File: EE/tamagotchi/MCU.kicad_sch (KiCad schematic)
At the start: 0 parts

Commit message: Minor Update pre Display add
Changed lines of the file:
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@@
 	(generator_version "9.0")
 	(paper "A4")
+	(label "MOSI"
+		(at 273.05 40.64 180)
+		(effects
+			(font
+				(size 1.27 1.27)
+			)
+			(justify right bottom)
+		)
+	)
 	(label "VAPE_EN"
 		(at 273.05 25.4 180)
@@
 		)
 	)
+	(label "CS"
+		(at 273.05 45.72 180)
+		(effects
+			(font
+				(size 1.27 1.27)
+			)
+			(justify right bottom)
+		)
+	)
 	(label "CE_N"
 		(at 22.86 15.24 0)
@@
 		)
 	)
+	(label "SCK"
+		(at 273.05 43.18 180)
+		(effects
+			(font
+				(size 1.27 1.27)
+			)
+			(justify right bottom)
+		)
+	)
 	(label "RED_EN"
 		(at 273.05 22.86 180)
@@
 		)
 	)
+	(label "MISO"
+		(at 273.05 38.1 180)
+		(effects
+			(font
+				(size 1.27 1.27)
+			)
+			(justify right bottom)
+		)
+	)
+	(hierarchical_label "MOSI"
+		(shape input)
+		(at 273.05 40.64 0)
+		(fields_autoplaced yes)
+		(effects
+			(font
+				(size 1.27 1.27)
+			)
+			(justify left)
+		)
+		(property "Netclass" ""
+			(at 273.05 41.91 0)
+			(effects
+				(font
+					(size 1.27 1.27)
+					(italic yes)
+				)
+				(justify left)
+			)
+		)
+	)
 	(hierarchical_label "INT_N"
 		(shape input)
@@
 		)
 	)
+	(hierarchical_label "MISO"
+		(shape input)
+		(at 273.05 38.1 0)
+		(effects
+			(font
+				(size 1.27 1.27)
+			)
+			(justify left)
+		)
+	)
 	(hierarchical_label "YELLOW_EN"
 		(shape input)
@@
 		)
 	)
+	(hierarchical_label "SCK"
+		(shape input)
+		(at 273.05 43.18 0)
+		(fields_autoplaced yes)
+		(effects
+			(font
+				(size 1.27 1.27)
+			)
+			(justify left)
+		)
+		(property "Netclass" ""
+			(at 273.05 44.45 0)
+			(effects
+				(font
+					(size 1.27 1.27)
+					(italic yes)
+				)
+				(justify left)
+			)
+		)
+	)
+	(hierarchical_label "CS"
+		(shape input)
+		(at 273.05 45.72 0)
+		(fields_autoplaced yes)
+		(effects
+			(font
+				(size 1.27 1.27)
+			)
+			(justify left)
+		)
+		(property "Netclass" ""
+			(at 273.05 46.99 0)
+			(effects
+				(font
+					(size 1.27 1.27)
+					(italic yes)
+				)
+				(justify left)
+			)
+		)
+	)

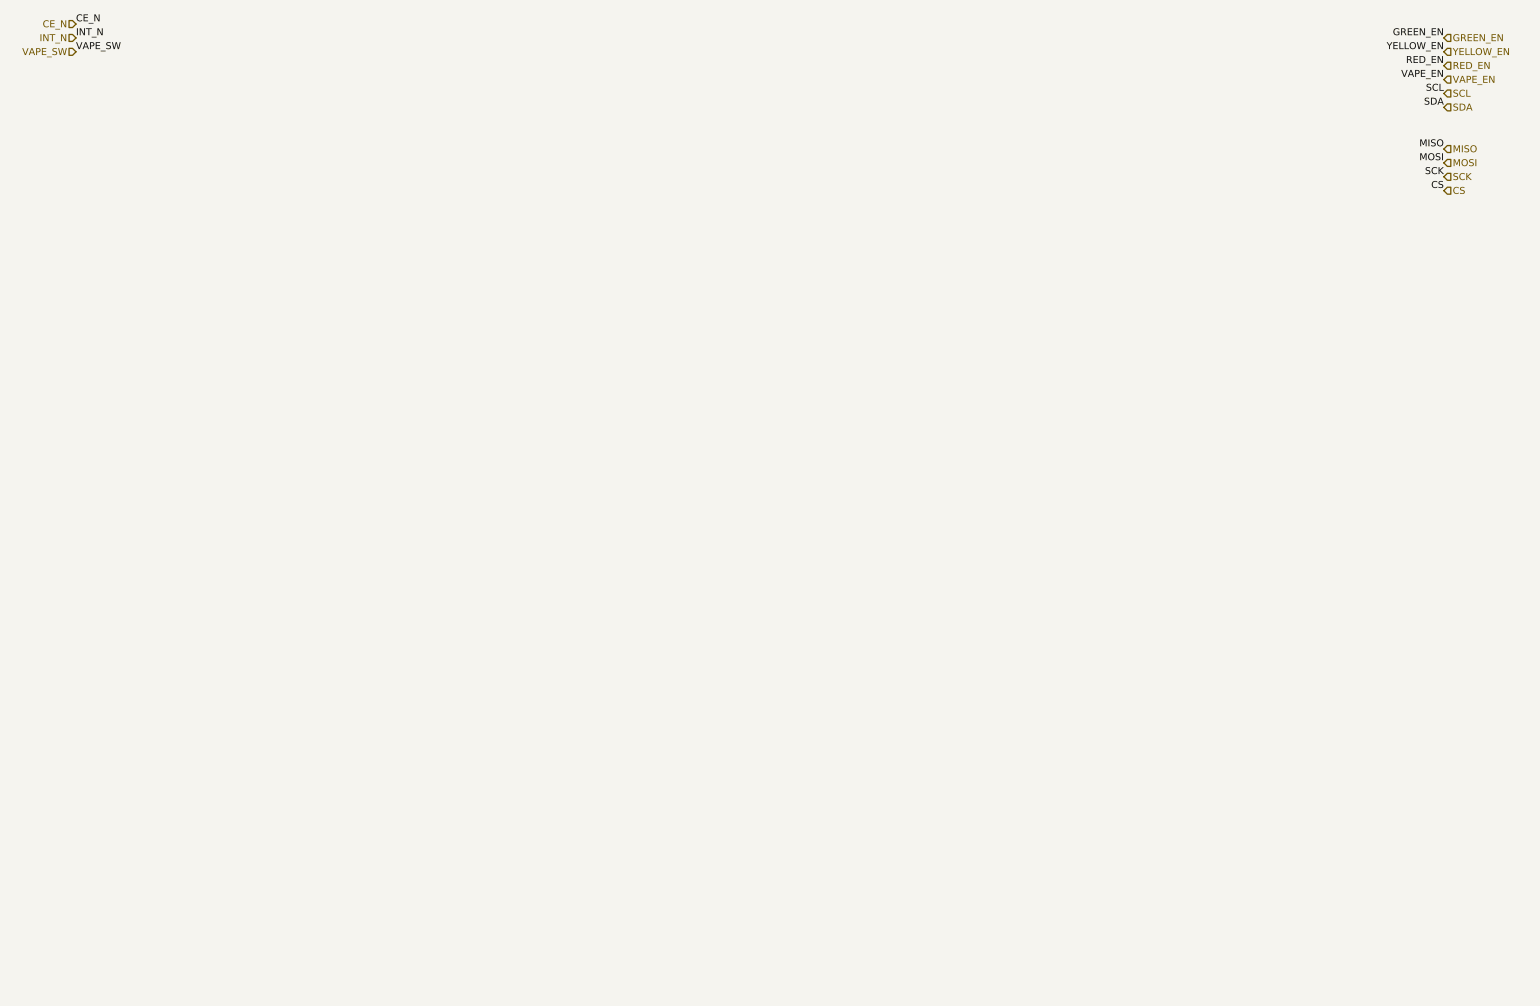
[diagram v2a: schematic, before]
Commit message: WIP - added 3D / footprints for devices. RGY LEDs aren't right
Need to do more outling / ect. super rough placement for everything.
LED footprint for RGY appears just wrong
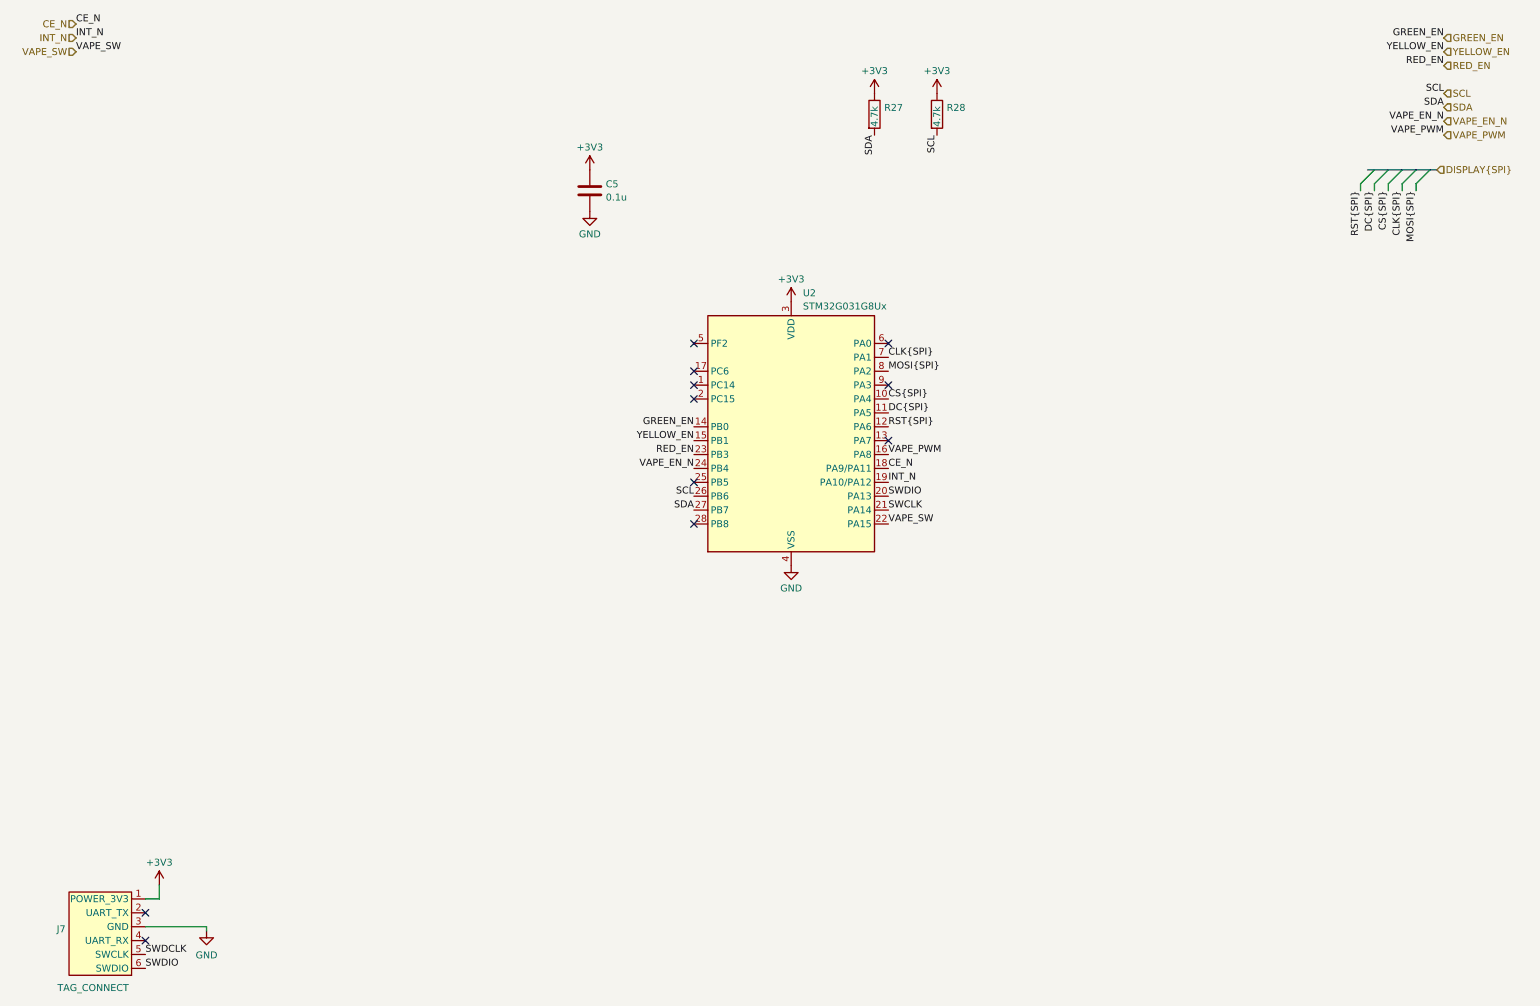
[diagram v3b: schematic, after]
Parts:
- added C5: 0.1u, Capacitor_SMD:C_0402_1005Metric_Pad0.74x0.62mm_HandSolder, symbol Device:C
- added J7: TAG_CONNECT, Connector:Tag-Connect_TC2030-IDC-FP_2x03_P1.27mm_Vertical, symbol ACTempDisconnect:TAG_CONNECT
- added R27, R28: 4.7k, Resistor_SMD:R_0402_1005Metric_Pad0.72x0.64mm_HandSolder, symbol Device:R
- added U2: STM32G031G8Ux, Package_DFN_QFN:QFN-28_4x4mm_P0.5mm, symbol MCU_ST_STM32G0:STM32G031G8Ux
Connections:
- net CE_N: now also U2.18 (PA9/PA11)
- net GREEN_EN: now also U2.14 (PB0)
- net INT_N: now also U2.19 (PA10/PA12)
- net RED_EN: now also U2.23 (PB3)
- net SCL: now also R28.2, U2.26 (PB6)
- net SDA: now also R27.2, U2.27 (PB7)
- net VAPE_SW: now also U2.22 (PA15)
- net YELLOW_EN: now also U2.15 (PB1)
- new net +3V3: C5.1, J7.1 (POWER_3V3), R27.1, R28.1, U2.3 (VDD)
- new net CLK{SPI}: U2.7 (PA1)
- new net CS{SPI}: U2.10 (PA4)
- new net DC{SPI}: U2.11 (PA5)
- new net GND: C5.2, J7.3 (GND), U2.4 (VSS)
- new net MOSI{SPI}: U2.8 (PA2)
- new net RST{SPI}: U2.12 (PA6)
- new net SWCLK: U2.21 (PA14)
- new net SWDCLK: J7.5 (SWCLK)
- new net SWDIO: J7.6 (SWDIO), U2.20 (PA13)
- new net VAPE_EN_N: U2.24 (PB4)
- new net VAPE_PWM: U2.16 (PA8)
- no-connect marks 0 -> 11

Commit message: Removed LEDs
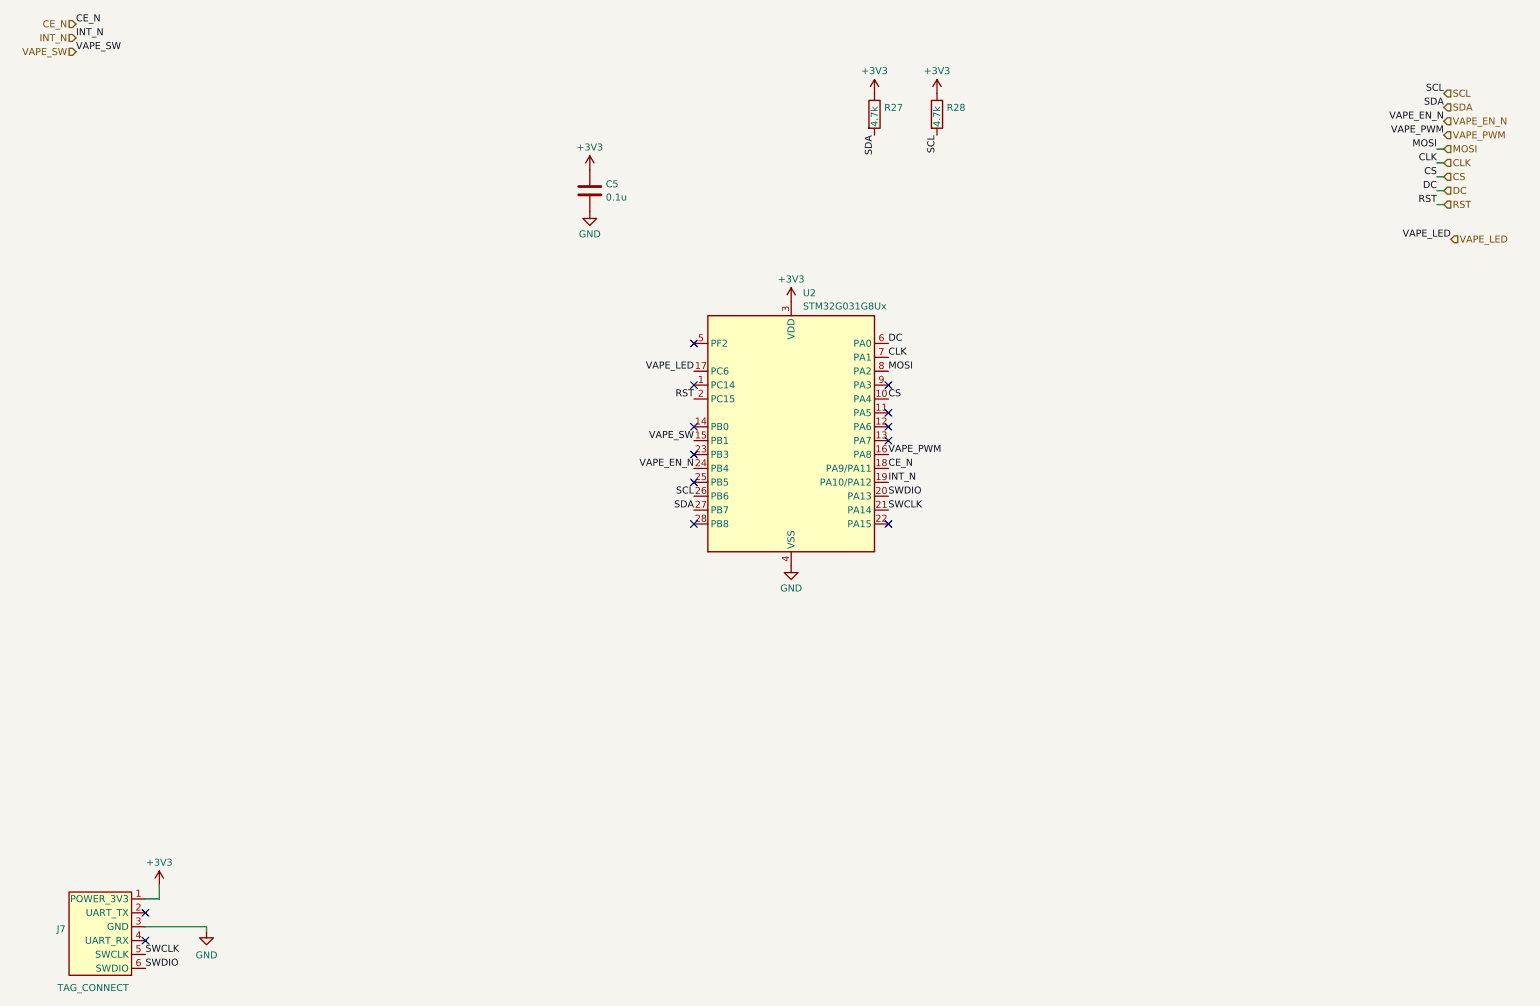
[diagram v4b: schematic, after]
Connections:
- net SWDCLK is gone; now on net SWCLK: J7.5 (SWCLK)
- net YELLOW_EN is gone; now on net VAPE_SW: U2.15 (PB1)
- net VAPE_SW: no longer U2.22 (PA15)
- net VAPE_LED: now reaches U2.17 (PC6)
- net RST: now reaches U2.2 (PC15)
- net DC: now reaches U2.6 (PA0)
- net CLK{SPI} renamed CLK
- net CS{SPI} renamed CS
- net DC{SPI}: no longer names the net of U2.11 (PA5)
- net GREEN_EN: no longer names the net of U2.14 (PB0)
- net MOSI{SPI} renamed MOSI
- net RED_EN: no longer names the net of U2.23 (PB3)
- net RST{SPI}: no longer names the net of U2.12 (PA6)
- no-connect marks 11 -> 13

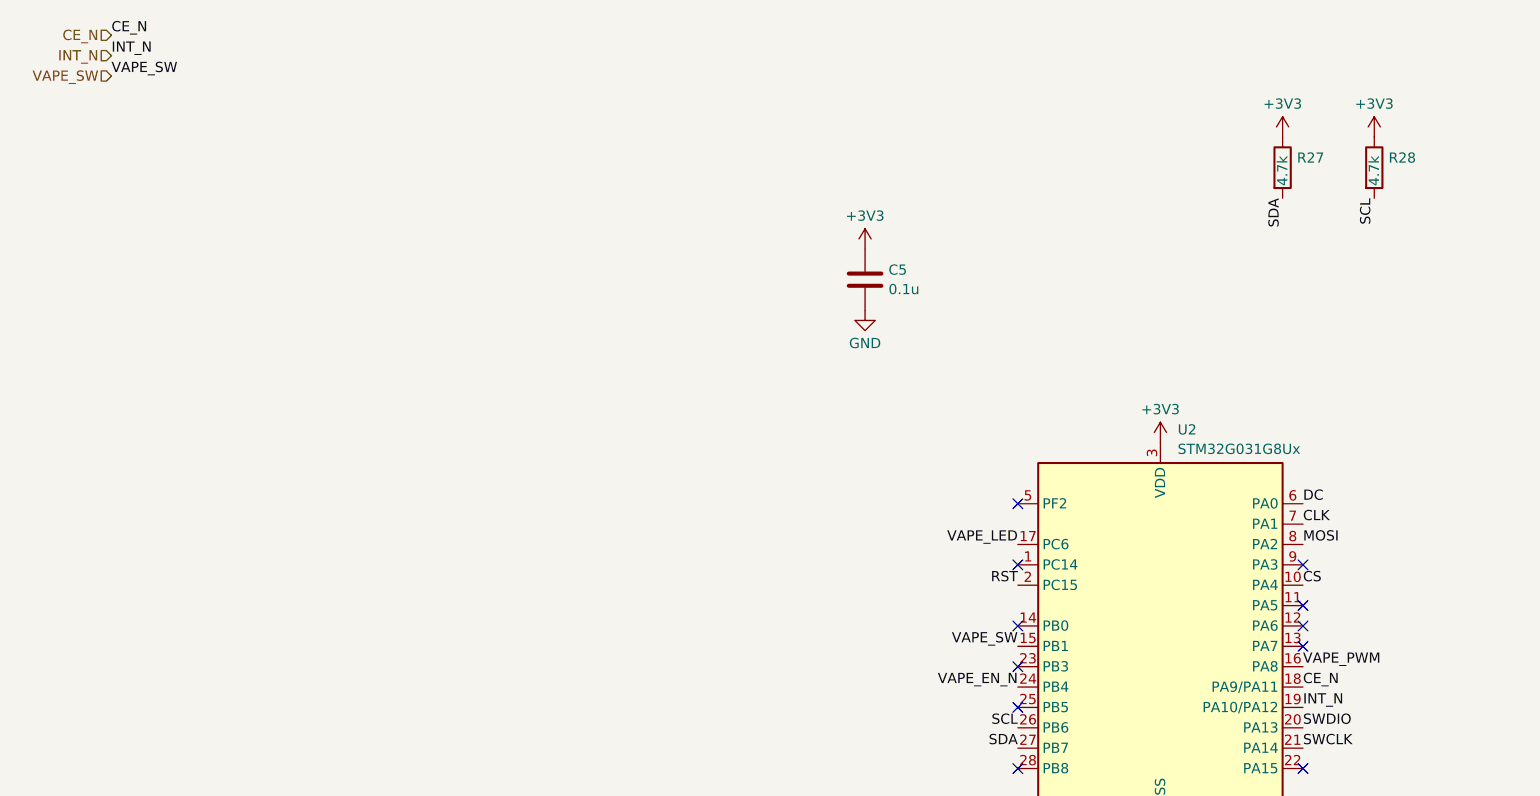
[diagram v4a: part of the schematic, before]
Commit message: First pass routing / placement & LED -> Buzzer for warning
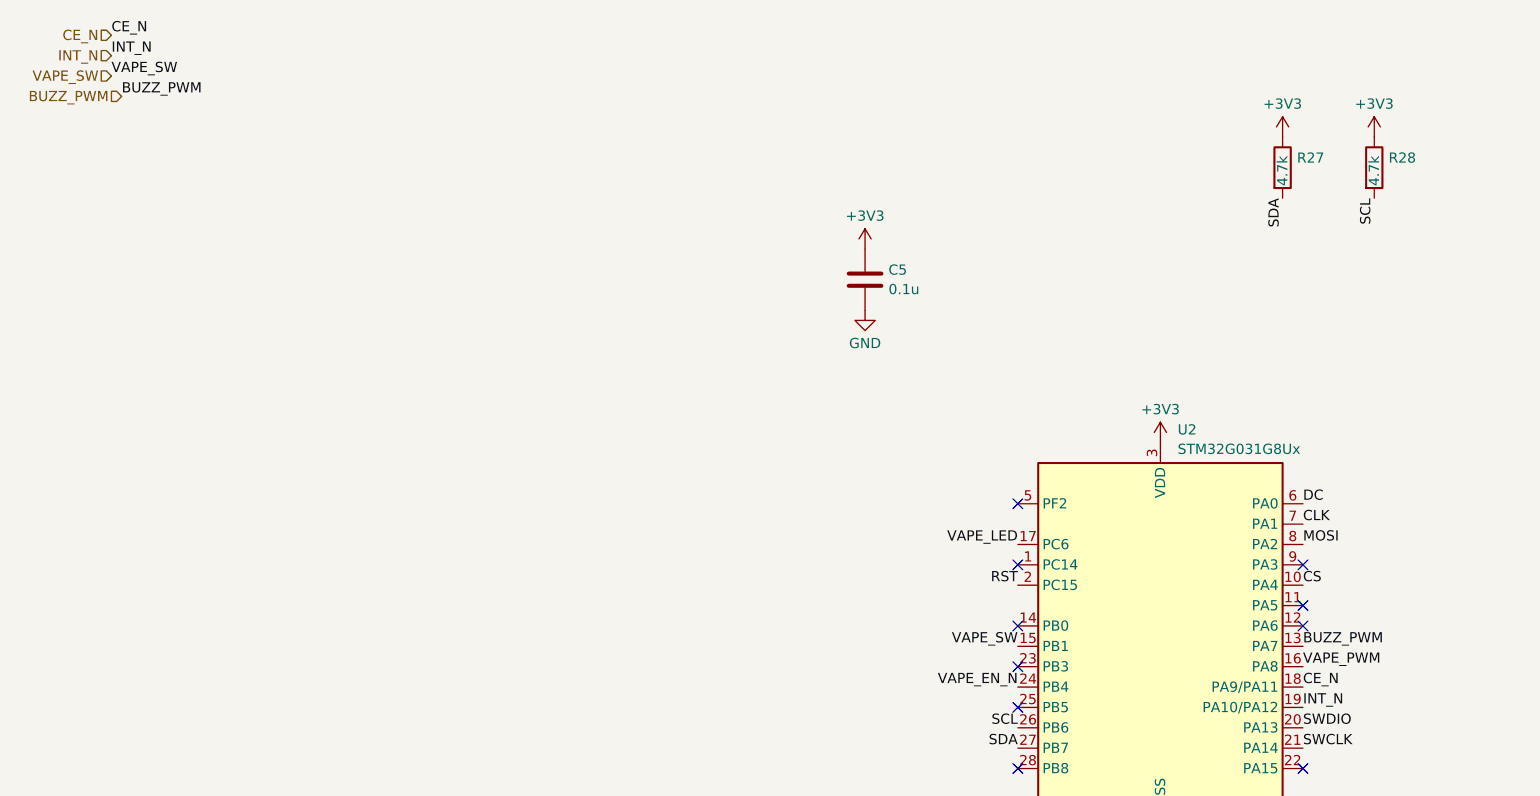
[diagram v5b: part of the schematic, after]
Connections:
- net BUZZ_PWM: now reaches U2.13 (PA7)
- no-connect marks 13 -> 12
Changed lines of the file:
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@@
-	)
-	(no_connect
-		(at 171.45 91.44)
 	)
 	(no_connect
@@
 			)
 			(justify right bottom)
+		)
+	)
+	(label "BUZZ_PWM"
+		(at 171.45 91.44 0)
+		(effects
+			(font
+				(size 1.27 1.27)
+			)
+			(justify left bottom)
+		)
+	)
+	(label "BUZZ_PWM"
+		(at 24.13 22.86 0)
+		(effects
+			(font
+				(size 1.27 1.27)
+			)
+			(justify left bottom)
 		)
 	)
@@
 		(effects
 			(font
+				(size 1.27 1.27)
+			)
+			(justify right)
+		)
+	)
+	(hierarchical_label "BUZZ_PWM"
+		(shape input)
+		(at 24.13 22.86 180)
+		(effects
+			(font
